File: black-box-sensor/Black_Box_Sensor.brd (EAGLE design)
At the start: 100 x 80 mm, 13 parts, among them U1 ADXL375, U2 ADXL375, U3 ATMEGA32U4-AU, U4 FXAS21002CQR1, U5 MIC5504-3.3YM5-TR, U6 NL27WZ32USG

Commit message: edit schematic
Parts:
- added C5: 0.1uF, rcl:C0603
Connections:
- new net CS1: U1.7, U6.2
- new net CS2: U6.6
- new net MISO: U1.12, U4.13
- new net MOSI: U4.12, U6.1, U6.5
- new net MOSI1: U1.13, U6.7
- new net MOSI2: U6.3
- new net SCLK: U1.14, U4.11
- net 3.3V: now also C5.1, U6.8
- net GND: now also C5.2, U6.4
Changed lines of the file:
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@@
 <attribute name="VALUE" x="-11.16" y="-127.73" size="1" layer="27" font="vector" rot="SR0" align="top-left"/>
+</element>
+<element name="C5" library="rcl" library_urn="urn:adsk.eagle:library:334" package="C0603" package3d_urn="urn:adsk.eagle:package:23616/2" value="0.1uF" x="-11.43" y="-132.08" smashed="yes">
+<attribute name="NAME" x="-12.065" y="-131.445" size="1.27" layer="25"/>
+<attribute name="POPULARITY" value="37" x="-11.43" y="-132.08" size="1.778" layer="27" display="off"/>
+<attribute name="SPICEPREFIX" value="C" x="-11.43" y="-132.08" size="1.778" layer="27" display="off"/>
+<attribute name="VALUE" x="-12.065" y="-133.985" size="1.27" layer="27"/>
 </element>
 </elements>
@@
 <contactref element="C6" pad="2"/>
 <contactref element="C11" pad="2"/>
+<contactref element="C5" pad="2"/>
+<contactref element="U6" pad="4"/>
+<wire x1="-11.56" y1="-126.48" x2="-10.58" y2="-132.08" width="0" layer="19" extent="1-1"/>
+<wire x1="-10.58" y1="-119.38" x2="-11.56" y2="-126.48" width="0" layer="19" extent="1-1"/>
 <wire x1="-10.58" y1="-115.57" x2="-10.58" y2="-119.38" width="0" layer="19" extent="1-1"/>
 <wire x1="-10.555" y1="-110.49" x2="-10.58" y2="-115.57" width="0" layer="19" extent="1-1"/>
 <wire x1="-10.555" y1="-106.68" x2="-10.555" y2="-110.49" width="0" layer="19" extent="1-1"/>
 <wire x1="-10.58" y1="-86.36" x2="-10.555" y2="-106.68" width="0" layer="19" extent="1-1"/>
-<wire x1="13.12" y1="15.24" x2="-10.58" y2="-86.36" width="0" layer="19" extent="1-1"/>
-<wire x1="19.05" y1="21.17" x2="13.12" y2="15.24" width="0" layer="19" extent="1-1"/>
-<wire x1="-11.4554" y1="-46.99" x2="19.05" y2="21.17" width="0" layer="19" extent="1-1"/>
-<wire x1="14.23" y1="16.875" x2="-11.4554" y2="-46.99" width="0" layer="19" extent="1-1"/>
-<wire x1="14.23" y1="17.375" x2="14.23" y2="16.875" width="0" layer="19" extent="1-1"/>
-<wire x1="14.23" y1="17.875" x2="14.23" y2="17.375" width="0" layer="19" extent="1-1"/>
-<wire x1="15.005" y1="20.15" x2="14.23" y2="19.875" width="0" layer="19" extent="1-1"/>
-<wire x1="15.505" y1="20.15" x2="15.005" y2="20.15" width="0" layer="19" extent="1-1"/>
-<wire x1="16.005" y1="20.15" x2="15.505" y2="20.15" width="0" layer="19" extent="1-1"/>
-<wire x1="16.505" y1="20.15" x2="16.005" y2="20.15" width="0" layer="19" extent="1-1"/>
-<wire x1="17.005" y1="20.15" x2="16.505" y2="20.15" width="0" layer="19" extent="1-1"/>
-<wire x1="15.505" y1="16.6" x2="14.23" y2="16.875" width="0" layer="19" extent="1-1"/>
-<wire x1="16.005" y1="16.6" x2="15.505" y2="16.6" width="0" layer="19" extent="1-1"/>
-<wire x1="-4.9075" y1="4.35" x2="15.005" y2="20.15" width="0" layer="19" extent="1-1"/>
+<wire x1="-11.4554" y1="-46.99" x2="-10.58" y2="-86.36" width="0" layer="19" extent="1-1"/>
+<wire x1="-4.9075" y1="4.35" x2="-11.4554" y2="-46.99" width="0" layer="19" extent="1-1"/>
 <wire x1="-4.9075" y1="5.15" x2="-4.9075" y2="4.35" width="0" layer="19" extent="1-1"/>
 <wire x1="-4.9075" y1="5.95" x2="-4.9075" y2="5.15" width="0" layer="19" extent="1-1"/>
 <wire x1="-4.9075" y1="7.55" x2="-4.9075" y2="5.95" width="0" layer="19" extent="1-1"/>
+<wire x1="13.12" y1="15.24" x2="-4.9075" y2="7.55" width="0" layer="19" extent="1-1"/>
+<wire x1="14.23" y1="16.875" x2="13.12" y2="15.24" width="0" layer="19" extent="1-1"/>
+<wire x1="14.23" y1="17.375" x2="14.23" y2="16.875" width="0" layer="19" extent="1-1"/>
+<wire x1="14.23" y1="17.875" x2="14.23" y2="17.375" width="0" layer="19" extent="1-1"/>
+<wire x1="17.005" y1="20.15" x2="17.78" y2="19.875" width="0" layer="19" extent="1-1"/>
+<wire x1="16.505" y1="20.15" x2="17.005" y2="20.15" width="0" layer="19" extent="1-1"/>
+<wire x1="16.005" y1="20.15" x2="16.505" y2="20.15" width="0" layer="19" extent="1-1"/>
+<wire x1="15.505" y1="20.15" x2="16.005" y2="20.15" width="0" layer="19" extent="1-1"/>
+<wire x1="15.005" y1="20.15" x2="15.505" y2="20.15" width="0" layer="19" extent="1-1"/>
+<wire x1="15.505" y1="16.6" x2="14.23" y2="16.875" width="0" layer="19" extent="1-1"/>
+<wire x1="16.005" y1="16.6" x2="15.505" y2="16.6" width="0" layer="19" extent="1-1"/>
+<wire x1="19.05" y1="21.17" x2="17.78" y2="19.875" width="0" layer="19" extent="1-1"/>
 </signal>
 <signal name="VBATT">
@@
 <contactref element="U4" pad="15"/>
 <contactref element="C3" pad="1"/>
-<contactref element="U4" pad="8"/>
 <contactref element="U4" pad="18"/>
 <contactref element="C4" pad="1"/>
 <contactref element="C11" pad="1"/>
 <contactref element="C12" pad="1"/>
+<contactref element="U4" pad="8"/>
 <contactref element="U4" pad="4"/>
+<contactref element="U6" pad="8"/>
+<contactref element="C5" pad="1"/>
+<wire x1="-8.76" y1="-124.98" x2="-12.28" y2="-132.08" width="0" layer="19" extent="1-1"/>
+<wire x1="-12.28" y1="-119.38" x2="-8.76" y2="-124.98" width="0" layer="19" extent="1-1"/>
 <wire x1="-12.28" y1="-115.57" x2="-12.28" y2="-119.38" width="0" layer="19" extent="1-1"/>
 <wire x1="-12.305" y1="-110.49" x2="-12.28" y2="-115.57" width="0" layer="19" extent="1-1"/>
@@
 <wire x1="17.78" y1="18.375" x2="-12.28" y2="-86.36" width="0" layer="19" extent="1-1"/>
 </signal>
+<signal name="CS1">
+<contactref element="U1" pad="7"/>
+<contactref element="U6" pad="2"/>
+<wire x1="-3.81" y1="4.2525" x2="-11.56" y2="-125.48" width="0" layer="19" extent="1-1"/>
+</signal>
+<signal name="SCLK">
+<contactref element="U1" pad="14"/>
+<contactref element="U4" pad="11"/>
+<wire x1="-3.81" y1="8.4475" x2="16.505" y2="16.6" width="0" layer="19" extent="1-1"/>
+</signal>
+<signal name="MOSI1">
+<contactref element="U1" pad="13"/>
+<contactref element="U6" pad="7"/>
+<wire x1="-2.7125" y1="6.75" x2="-8.76" y2="-125.48" width="0" layer="19" extent="1-1"/>
+</signal>
+<signal name="MISO">
+<contactref element="U1" pad="12"/>
+<contactref element="U4" pad="13"/>
+<wire x1="-2.7125" y1="8.35" x2="17.78" y2="16.875" width="0" layer="19" extent="1-1"/>
+</signal>
+<signal name="MOSI">
+<contactref element="U6" pad="1"/>
+<contactref element="U6" pad="5"/>
+<contactref element="U4" pad="12"/>
+<wire x1="-8.76" y1="-126.48" x2="-11.56" y2="-124.98" width="0" layer="19" extent="1-1"/>
+<wire x1="17.005" y1="16.6" x2="-11.56" y2="-124.98" width="0" layer="19" extent="1-1"/>
+</signal>
+<signal name="CS2">
+<contactref element="U6" pad="6"/>
+</signal>
+<signal name="MOSI2">
+<contactref element="U6" pad="3"/>
+</signal>
 </signals>

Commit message: add to bbs schematic
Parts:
- added C10, C9: 1µF, rcl:C0603
- added C7, C8: 0.1uF, rcl:C0603
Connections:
- new net CS3: U4.17
- net 3.3V: now also C10.1, C7.1, C8.1, C9.1, U2.1, U3.14, U3.24, U3.34, U3.44, U3.6
- net CS1: now also U3.8
- net CS2: now also U2.7, U3.12
- net GND: now also C10.2, C7.2, C8.2, C9.2, U2.2, U2.4, U2.5, U2.6, U3.15, U3.23, U3.35, U3.43, U3.5
- net MISO: now also U2.12, U3.11
- net MOSI: now also U3.10
- net MOSI2: now also U2.13
- net SCLK: now also U2.14, U3.9

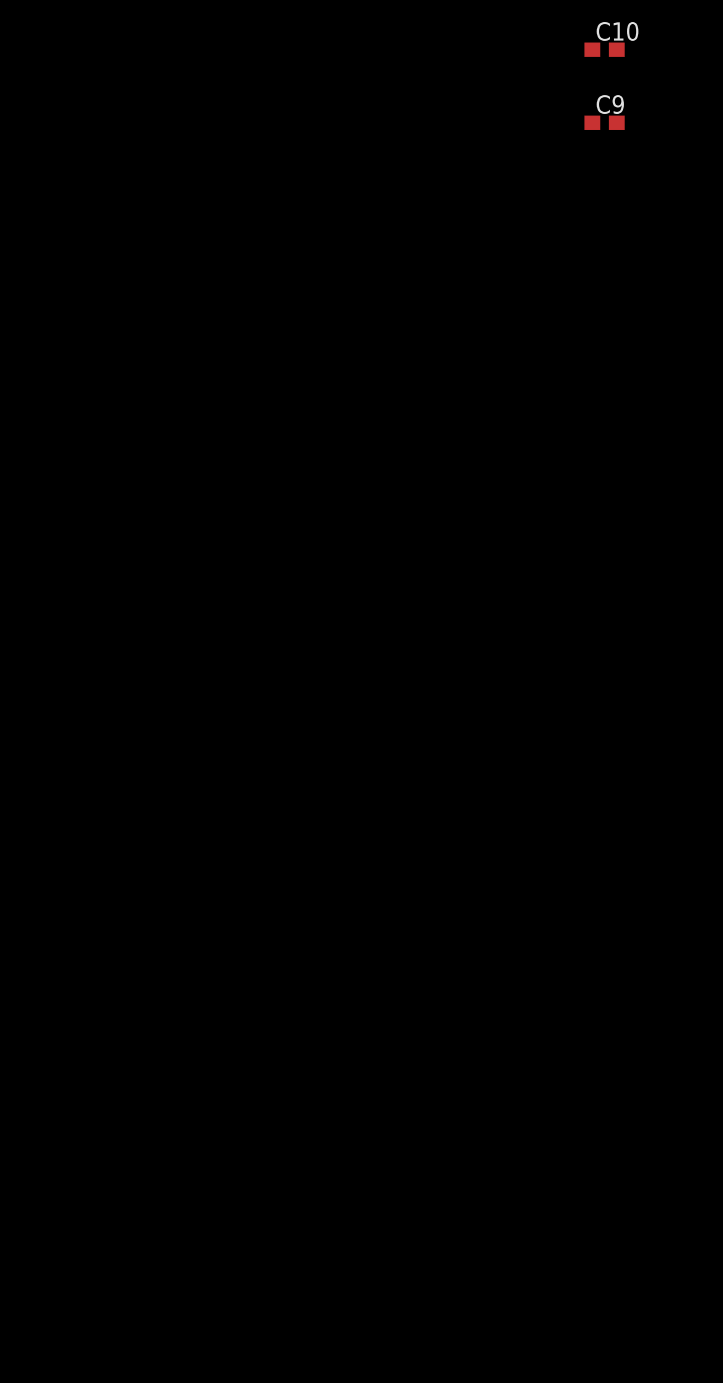
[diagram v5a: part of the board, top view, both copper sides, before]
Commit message: add us and sd card reader
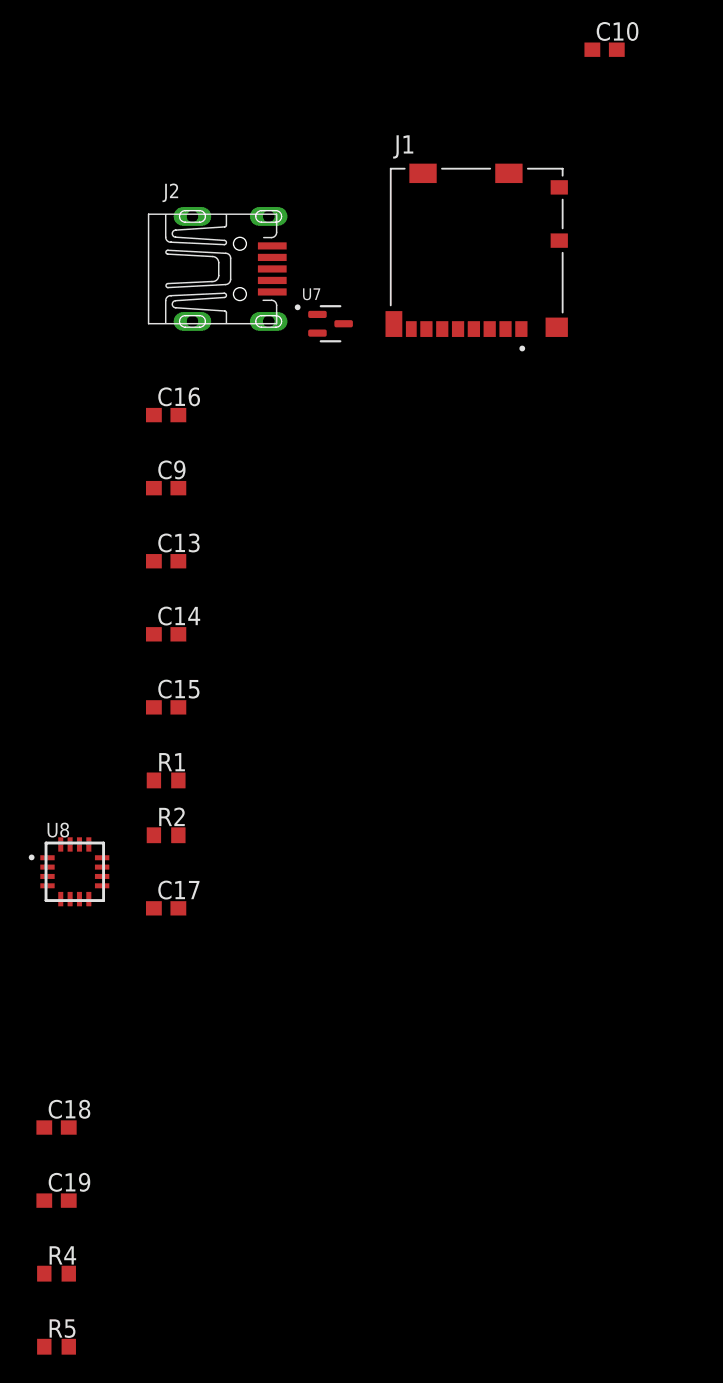
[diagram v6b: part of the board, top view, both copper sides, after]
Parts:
- added C13, C14, C15, C16, C17, C18, C19: 0.1uF, rcl:C0603
- added J1: 104031-0811, BBS_Library:MOLEX_104031-0811
- added J2: UX60-MB-5S8, BBS_Library:UX60-MB-5S8
- added R1, R2: 22, rcl:R0603
- added R4, R5: 499, rcl:R0603
- added U7: MAX7375AXR805T, BBS_Library:SOT65P210X110-3N
- added U8: AD8426ACPZ-WP, BBS_Library:16LFCSP
- C9: value 1µF -> 0.1uF
- moved C9 39.7 mm to (-41.9, -182.9)
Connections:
- new net ADC9: U3.26, U8.15
- new net CS4: J1.2, U3.22
- new net D+: J2.3, R2.1, R2.2, U3.4
- new net D-: J2.4, R1.1, R1.2, U3.3
- new net INT0: U1.8, U3.18
- new net INT1: U1.9, U3.19
- new net INT2: U2.8, U3.20
- new net INT3: U2.9, U3.21
- new net N$4: R4.2, R5.1, U8.9
- new net VBUS: J2.5, U3.7
- new net VREF/2: U8.12, U8.14, U8.6
- new net XTAL1: U3.17, U7.2
- net 3.3V: now also C13.1, C14.1, C15.1, C16.1, C17.1, C18.1, C19.1, J1.4, R5.2, U3.13, U7.1, U8.16, U8.5
- net CS3: now also U3.25
- net GND: now also C13.2, C14.2, C15.2, C16.2, C17.2, C18.2, C19.2, J1.6, J1.G1, J1.G2, J1.G3, J1.G4, J2.1, R4.1, U7.3, U8.13, U8.8
- net MISO: now also J1.7
- net MOSI: now also J1.3
- net SCLK: now also J1.5

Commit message: finish schematic for bbs
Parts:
- added J3: B4B-PH-SM4-TBT(LF)(SN), BBS_Library:CONN_B4B-PH-SM4-TB_JST
- moved R5 307.2 mm to (87.5, 32.4)
- moved R4 301.0 mm to (83.5, 32.5)
- moved C19 293.8 mm to (85.5, 28.6)
- moved C18 286.8 mm to (85.5, 25.7)
- moved R2 276.4 mm to (49.1, 54.0)
- moved U8 274.2 mm to (78.7, 33.5)
- moved C17 271.6 mm to (73.1, 33.9)
- moved C13 269.5 mm to (68.1, 58.0)
- moved C14 269.5 mm to (68.1, 53.0)
- moved C16 269.5 mm to (68.1, 68.2)
- moved C9 269.5 mm to (68.1, 63.1)
- moved J2 269.5 mm to (66.8, 78.4)
- moved R1 269.5 mm to (68.1, 42.8)
- moved U7 269.5 mm to (79.5, 74.5)
- moved C15 240.7 mm to (51.1, 23.9)
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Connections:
- new net V+: J3.2, U8.4
- new net V-: J3.3, U8.1
- net 3.3V: now also J3.1
- net GND: now also J3.4, J3.5, J3.6

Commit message: update black box sensor
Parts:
- added CN1: (no value), Hocki_Library:JST-PH-2-SMT
- added LED1: (no value), led:CHIP-LED0805
- added LED2: (no value), led:KA-3528ASYC
- added R3, R6: 100, rcl:R0603
- moved U7 67.2 mm to (32.5, 26.5), turned to 90 degrees
- moved C17 60.0 mm to (16.9, 12.9), turned to 270 degrees
- moved J1 54.6 mm to (7.38, 14.5)
- moved C13 50.0 mm to (38.2, 17.9), turned to 180 degrees
- moved C19 47.9 mm to (40.2, 12.8), turned to 90 degrees
- moved R5 47.3 mm to (42.9, 16.8), turned to 180 degrees
- moved J2 46.5 mm to (35.4, 44.2), turned to 270 degrees
- moved U2 45.6 mm to (9.86, 26.4), turned to 271.1 degrees
- moved U1 44.0 mm to (9.86, 32.1), turned to 270 degrees
- moved C9 43.7 mm to (51.4, 22.7), turned to 90 degrees
- moved U6 42.0 mm to (3.79, 30.5), turned to 270 degrees
- moved C16 41.9 mm to (51.5, 29.7), turned to 270 degrees
- moved R4 40.7 mm to (46.0, 16.8), turned to 180 degrees
- moved C14 40.6 mm to (36.1, 28.0), turned to 270 degrees
- moved U8 40.0 mm to (44.5, 12.7), turned to 90 degrees
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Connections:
- removed net +3.3V: C2.1, U5.5
- removed net ADC9: U3.26, U8.15
- new net CURRENT: U3.27, U8.15
- new net LED: LED2.A, U3.26
- new net N$2: J2.3, R2.2
- new net N$3: J2.4, R1.2
- new net N$5: LED2.C, R3.2
- new net N$6: LED1.C, R6.1
- net 3.3V: now also C2.1, LED1.A, U5.5
- net D+: no longer J2.3, R2.2
- net D-: no longer J2.4, R1.2
- net GND: now also CN1.2, CN1.NC1, CN1.NC2, R3.1, R6.2
- net VBATT: now also CN1.1
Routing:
- net LED: track 0.00 -> 101.2 mm, vias 0 -> 1
- net MOSI: track 0.00 -> 91.9 mm, vias 0 -> 10
- net GND: track 0.00 -> 81.4 mm, vias 0 -> 45
- net SCLK: track 0.00 -> 78.1 mm, vias 0 -> 9
- net MISO: track 0.00 -> 74.5 mm, vias 0 -> 8
- net CS1: track 0.00 -> 51.0 mm, vias 0 -> 2
- net CS2: track 0.00 -> 48.6 mm, vias 0 -> 6
- net CS3: track 0.00 -> 39.9 mm, vias 0 -> 2
- net INT0: track 0.00 -> 37.6 mm, vias 0 -> 2
- net INT2: track 0.00 -> 34.4 mm, vias 0 -> 4
- net INT1: track 0.00 -> 33.5 mm, vias 0 -> 2
- net INT3: track 0.00 -> 32.9 mm, vias 0 -> 2
- net CS4: track 0.00 -> 27.5 mm, vias 0 -> 2
- net 3.3V: track 0.00 -> 22.7 mm, vias 0 -> 8
- net N$3: track 0.00 -> 18.0 mm
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- added copper zone on layer 1, net 3.3V
- added copper zone on layer 1, net GND
- added copper zone on layer 16, net GND
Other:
- board size 100 x 80 mm -> 53 x 44 mm
